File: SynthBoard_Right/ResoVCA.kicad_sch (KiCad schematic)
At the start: 23 parts, among them Q8 2SA812, U4 Opamp_Dual, U6 Opamp_Dual, U8 LM13700

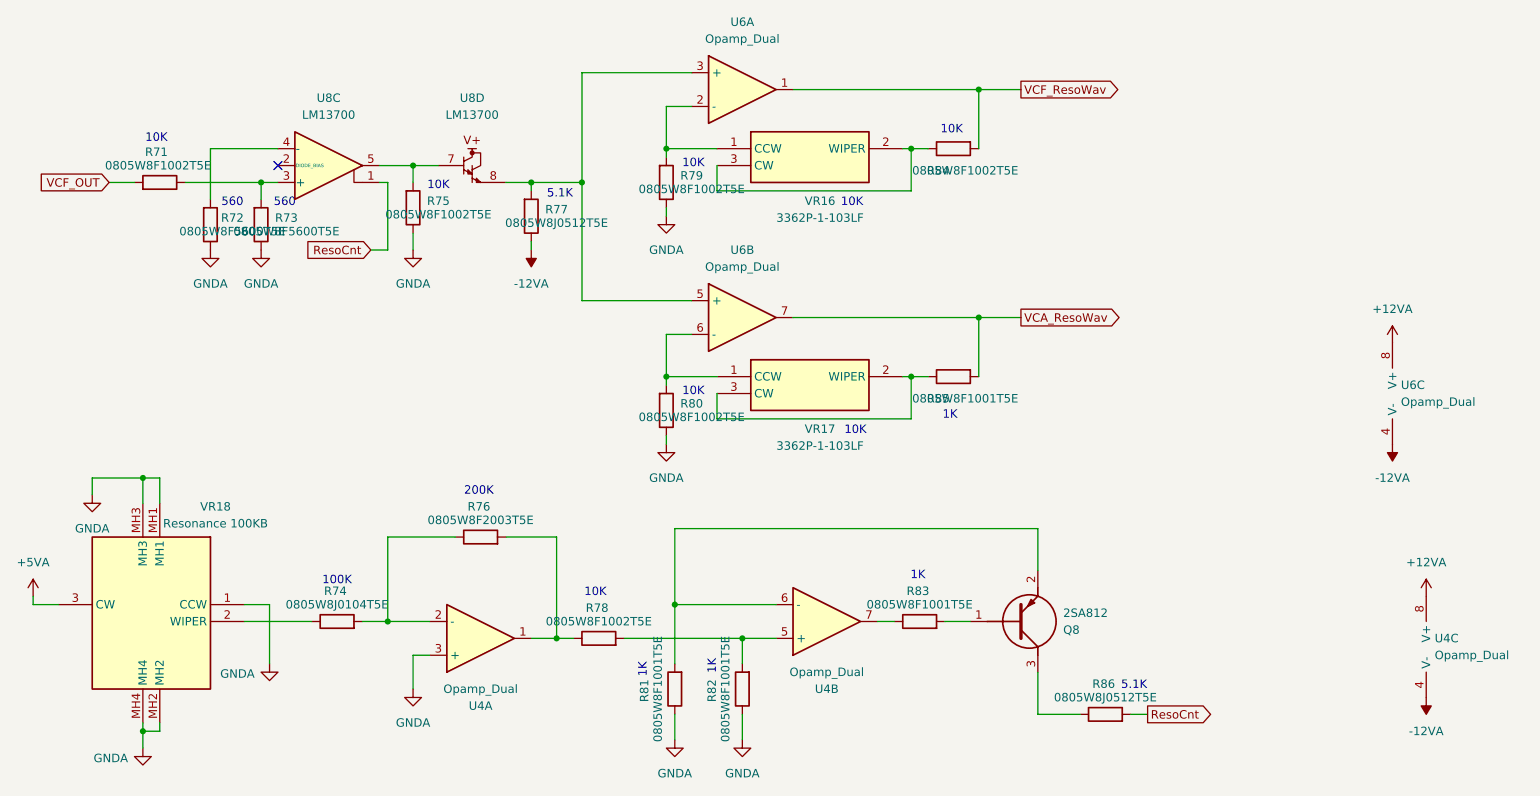
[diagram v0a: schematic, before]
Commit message: SynthBoard Right
配線ミスを修正
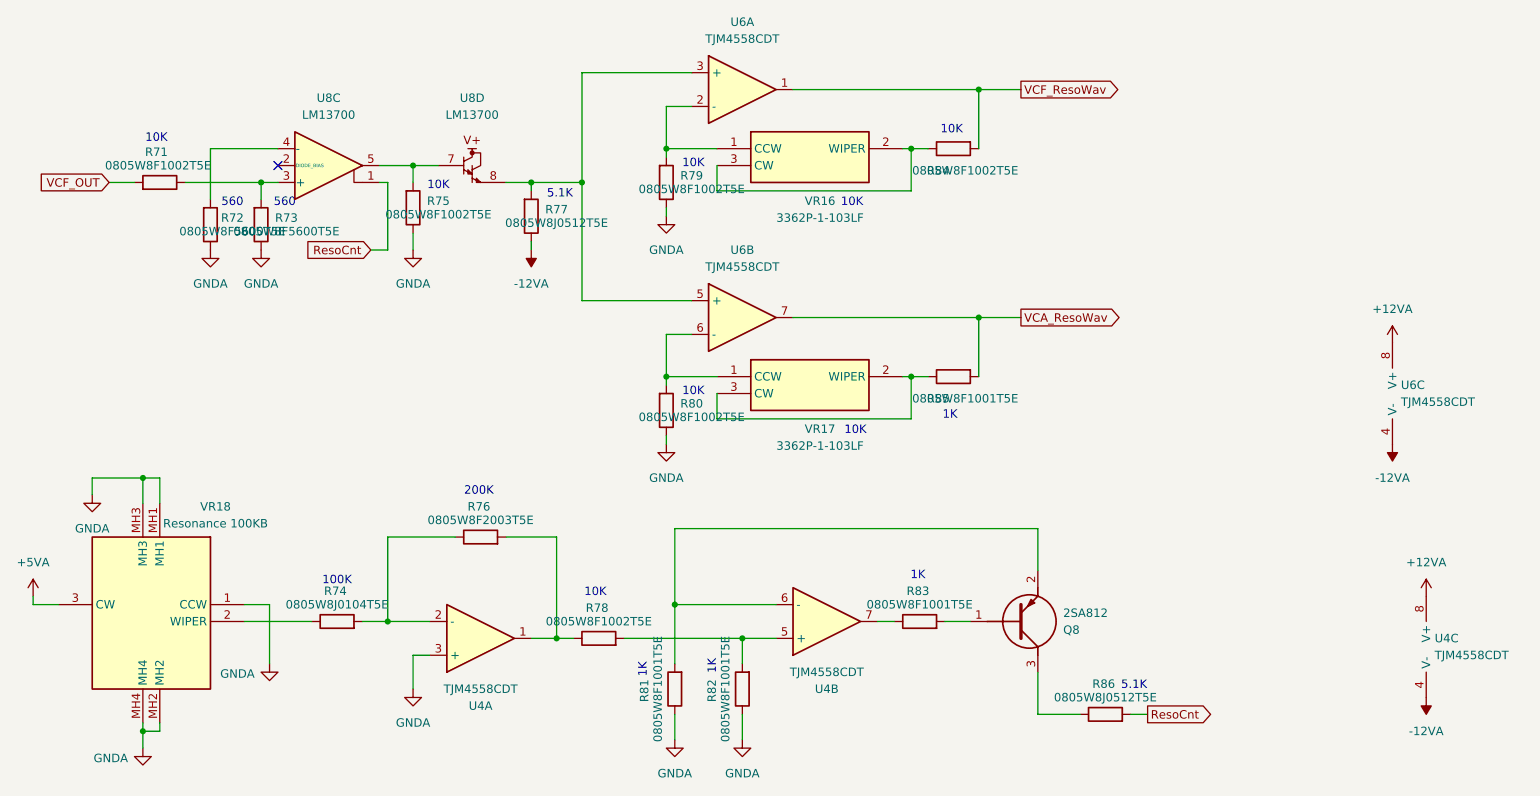
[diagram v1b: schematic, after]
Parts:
- U4, U6: value Opamp_Dual -> TJM4558CDT
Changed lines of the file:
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@@
 			)
 		)
-		(property "Value" "Opamp_Dual"
+		(property "Value" "TJM4558CDT"
 			(at 260.35 120.6499 0)
 			(effects
@@
 			)
 		)
-		(property "Value" "Opamp_Dual"
+		(property "Value" "TJM4558CDT"
 			(at 156.21 62.23 0)
 			(effects
@@
 			)
 		)
-		(property "Value" "Opamp_Dual"
+		(property "Value" "TJM4558CDT"
 			(at 168.91 123.19 0)
 			(effects
@@
 			)
 		)
-		(property "Value" "Opamp_Dual"
+		(property "Value" "TJM4558CDT"
 			(at 156.21 27.94 0)
 			(effects
@@
 			)
 		)
-		(property "Value" "Opamp_Dual"
+		(property "Value" "TJM4558CDT"
 			(at 255.27 82.5499 0)
 			(effects
@@
 			)
 		)
-		(property "Value" "Opamp_Dual"
+		(property "Value" "TJM4558CDT"
 			(at 116.84 125.73 0)
 			(effects

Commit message: SynthBoard Right
Basic部品で更新まで
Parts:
- R74: value 0805W8J0104T5E -> 0805W8F1003T5E
- R77, R86: value 0805W8J0512T5E -> 0805W8F5101T5E
- U4, U6: value TJM4558CDT -> TL072CDT
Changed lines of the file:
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@@
 			)
 		)
-		(property "Value" "0805W8J0104T5E"
+		(property "Value" "0805W8F1003T5E"
 			(at 95.25 113.03 90)
 			(effects
@@
 			)
 		)
-		(property "Value" "TJM4558CDT"
+		(property "Value" "TL072CDT"
 			(at 260.35 120.6499 0)
 			(effects
@@
 			)
 		)
-		(property "Value" "0805W8J0512T5E"
+		(property "Value" "0805W8F5101T5E"
 			(at 210.82 127 90)
 			(effects
@@
 			)
 		)
-		(property "Value" "0805W8J0512T5E"
+		(property "Value" "0805W8F5101T5E"
 			(at 128.27 55.626 0)
 			(effects
@@
 			)
 		)
-		(property "Value" "TJM4558CDT"
+		(property "Value" "TL072CDT"
 			(at 156.21 62.23 0)
 			(effects
@@
 			)
 		)
-		(property "Value" "TJM4558CDT"
+		(property "Value" "TL072CDT"
 			(at 168.91 123.19 0)
 			(effects
@@
 			)
 		)
-		(property "Value" "TJM4558CDT"
+		(property "Value" "TL072CDT"
 			(at 156.21 27.94 0)
 			(effects
@@
 			)
 		)
-		(property "Value" "TJM4558CDT"
+		(property "Value" "TL072CDT"
 			(at 255.27 82.5499 0)
 			(effects
@@
 			)
 		)
-		(property "Value" "TJM4558CDT"
+		(property "Value" "TL072CDT"
 			(at 116.84 125.73 0)
 			(effects

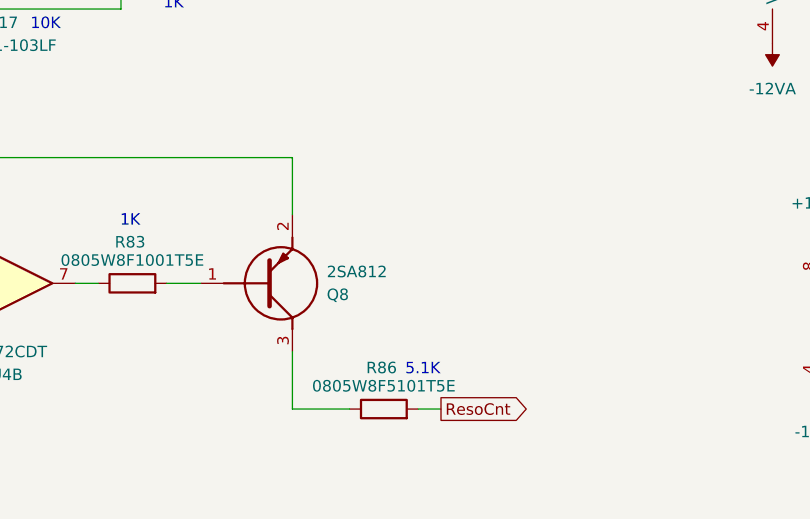
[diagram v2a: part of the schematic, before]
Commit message: MC2
まとめて登録
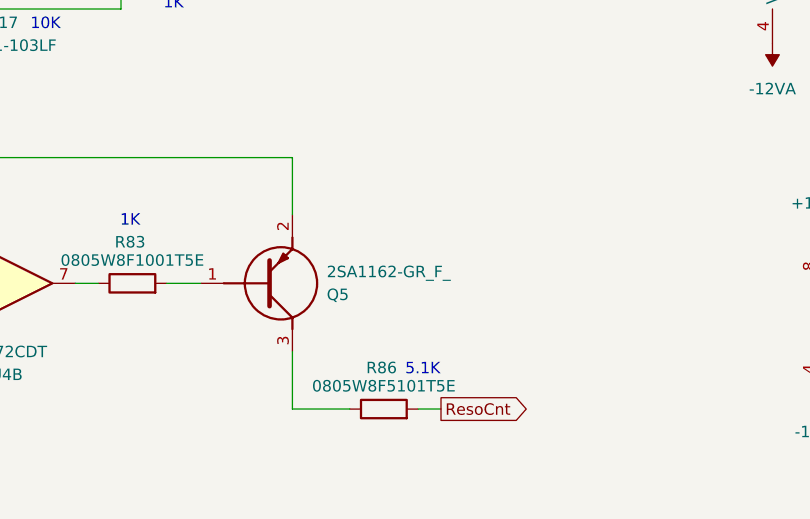
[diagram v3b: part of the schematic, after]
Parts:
- removed Q8: 2SA812, SamacSys_parts:SOT95P240X120-3N, symbol SamacSys_Parts:2SA812
- added Q5: 2SA1162-GR_F_, SamacSys_parts:1SS294LFT, symbol SamacSys_Parts:2SA1162-GR_F_
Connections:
- net at R83.2: now also Q5.1 (B)
- net at R81.2, U4.6 (-): now also Q5.2 (E)
- net at R86.1: now also Q5.3 (C)
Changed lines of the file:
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@@
-	)
-	(symbol
-		(lib_id "SamacSys_Parts:2SA812")
-		(at 190.5 115.57 0)
-		(mirror x)
-		(unit 1)
-		(exclude_from_sim no)
-		(in_bom yes)
-		(on_board yes)
-		(dnp no)
-		(property "Reference" "Q8"
-			(at 204.47 116.8401 0)
-			(effects
-				(font
-					(size 1.27 1.27)
-				)
-				(justify left)
-			)
-		)
-		(property "Value" "2SA812"
-			(at 204.47 114.3001 0)
-			(effects
-				(font
-					(size 1.27 1.27)
-				)
-				(justify left)
-			)
-		)
-		(property "Footprint" "SamacSys_parts:SOT95P240X120-3N"
-			(at 204.47 14.3 0)
-			(effects
-				(font
-					(size 1.27 1.27)
-				)
-				(justify left top)
-				(hide yes)
-			)
-		)
-		(property "Datasheet" "https://4donline.ihs.com/images/VipMasterIC/IC/GSCC/GSCC-S-A0010612759/GSCC-S-A0010613804-1.pdf?hkey=EF798316E3902B6ED9A73243A3159BB0"
-			(at 204.47 -85.7 0)
-			(effects
-				(font
-					(size 1.27 1.27)
-				)
-				(justify left top)
-				(hide yes)
-			)
-		)
-		(property "Description" "Silicon Epitaxial Planar Transistor,Commplementary to 2SC1623.  High DC current gain:hFE=200typ. (VCE=-6.0V,IC=-1.0mA)  High Voltage: VCEO=-50V."
-			(at 190.5 115.57 0)
-			(effects
-				(font
-					(size 1.27 1.27)
-				)
-				(hide yes)
-			)
-		)
-		(property "Height" "1.2"
-			(at 204.47 -285.7 0)
-			(effects
-				(font
-					(size 1.27 1.27)
-				)
-				(justify left top)
-				(hide yes)
-			)
-		)
-		(property "Manufacturer_Name" "Galaxy"
-			(at 204.47 -385.7 0)
-			(effects
-				(font
-					(size 1.27 1.27)
-				)
-				(justify left top)
-				(hide yes)
-			)
-		)
-		(property "Manufacturer_Part_Number" "2SA812"
-			(at 204.47 -485.7 0)
-			(effects
-				(font
-					(size 1.27 1.27)
-				)
-				(justify left top)
-				(hide yes)
-			)
-		)
-		(property "Mouser Part Number" ""
-			(at 204.47 -585.7 0)
-			(effects
-				(font
-					(size 1.27 1.27)
-				)
-				(justify left top)
-				(hide yes)
-			)
-		)
-		(property "Mouser Price/Stock" ""
-			(at 204.47 -685.7 0)
-			(effects
-				(font
-					(size 1.27 1.27)
-				)
-				(justify left top)
-				(hide yes)
-			)
-		)
-		(property "Arrow Part Number" ""
-			(at 204.47 -785.7 0)
-			(effects
-				(font
-					(size 1.27 1.27)
-				)
-				(justify left top)
-				(hide yes)
-			)
-		)
-		(property "Arrow Price/Stock" ""
-			(at 204.47 -885.7 0)
-			(effects
-				(font
-					(size 1.27 1.27)
-				)
-				(justify left top)
-				(hide yes)
-			)
-		)
-		(pin "3"
-		)
-		(pin "1"
-		)
-		(pin "2"
-		)
-		(instances
-			(project "SynthBoard"
-				(path "/92765e2f-a998-485f-b610-76a9d5b50cba/ce791b53-fe36-4133-8ad7-8aef41fe14ef"
-					(reference "Q8")
-					(unit 1)
-				)
-			)
-		)
 	)
 	(symbol
@@
 					(unit 1)
 				)
+			)
+		)
+	)
+	(symbol
+		(lib_id "SamacSys_Parts:2SA1162-GR_F_")
+		(at 190.5 115.57 0)
+		(mirror x)
+		(unit 1)
+		(exclude_from_sim no)
+		(in_bom yes)
+		(on_board yes)
+		(dnp no)
+		(property "Reference" "Q5"
+			(at 204.47 116.8401 0)
+			(effects
+				(font
+					(size 1.27 1.27)
+				)
+				(justify left)
+			)
+		)
+		(property "Value" "2SA1162-GR_F_"
+			(at 204.47 114.3001 0)
+			(effects
+				(font
+					(size 1.27 1.27)
+				)
+				(justify left)
+			)
+		)
+		(property "Footprint" "SamacSys_parts:1SS294LFT"
+			(at 204.47 14.3 0)
+			(effects
+				(font
+					(size 1.27 1.27)
+				)
+				(justify left top)
+				(hide yes)
+			)
+		)
+		(property "Datasheet" "https://toshiba.semicon-storage.com/ap-en/product/bipolar-transistor/bipolar-transistor/detail.2SA1162.html"
+			(at 204.47 -85.7 0)
+			(effects
+				(font
+					(size 1.27 1.27)
+				)
+				(justify left top)
+				(hide yes)
+			)
+		)
+		(property "Description" "Transistor Toshiba 2SA1162-GR(F) PNP Bipolar Transistor, 0.15 A, 50 V, 3-Pin SC-59"
+			(at 190.5 115.57 0)
+			(effects
+				(font
+					(size 1.27 1.27)
+				)
+				(hide yes)
+			)
+		)
+		(property "Height" "1.4"
+			(at 204.47 -285.7 0)
+			(effects
+				(font
+					(size 1.27 1.27)
+				)
+				(justify left top)
+				(hide yes)
+			)
+		)
+		(property "Manufacturer_Name" "Toshiba"
+			(at 204.47 -385.7 0)
+			(effects
+				(font
+					(size 1.27 1.27)
+				)
+				(justify left top)
+				(hide yes)
+			)
+		)
+		(property "Manufacturer_Part_Number" "2SA1162-GR(F)"
+			(at 204.47 -485.7 0)
+			(effects
+				(font
+					(size 1.27 1.27)
+				)
+				(justify left top)
+				(hide yes)
+			)
+		)
+		(property "Mouser Part Number" ""
+			(at 204.47 -585.7 0)
+			(effects
+				(font
+					(size 1.27 1.27)
+				)
+				(justify left top)
+				(hide yes)
+			)
+		)
+		(property "Mouser Price/Stock" ""
+			(at 204.47 -685.7 0)
+			(effects
+				(font
+					(size 1.27 1.27)
+				)
+				(justify left top)
+				(hide yes)
+			)
+		)
+		(property "Arrow Part Number" ""
+			(at 204.47 -785.7 0)
+			(effects
+				(font
+					(size 1.27 1.27)
+				)
+				(justify left top)
+				(hide yes)
+			)
+		)
+		(property "Arrow Price/Stock" ""
+			(at 204.47 -885.7 0)
+			(effects
+				(font
+					(size 1.27 1.27)
+				)
+				(justify left top)
+				(hide yes)
+			)
+		)
+		(pin "1"
+		)
+		(pin "2"
+		)
+		(pin "3"
+		)
+		(instances
+			(project "SynthBoard"
+				(path "/92765e2f-a998-485f-b610-76a9d5b50cba/ce791b53-fe36-4133-8ad7-8aef41fe14ef"
+					(reference "Q5")
+					(unit 1)
+				)
